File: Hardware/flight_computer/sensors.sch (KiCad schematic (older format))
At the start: 21 parts

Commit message: added components, rerranged things to slow down dan
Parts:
- removed C?: C_10u, Capacitors_SMD:C_0805, symbol openDrone_parts:C_10u
- removed C?: C_0u1, Capacitors_SMD:C_0805, symbol openDrone_parts:C_0u1
- removed C?: C_2u2, Capacitors_SMD:C_0805, symbol openDrone_parts:C_2u2
- removed FL?: EMI_Filter_CLC_100MHZ, drone_footprints:NFL21SP107X1C3D, symbol openDrone_parts:EMI_Filter_CLC_100MHZ
- removed R?: R_220, Resistors_SMD:R_0805, symbol openDrone_parts:R_220
- removed U?: LP5907QMFX-3.3, TO_SOT_Packages_SMD:SOT-23-5, symbol openDrone_parts:LP5907QMFX-3.3
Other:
- note added: "BATTERY = VBAT\nBUCK CONVERTER OUTPUT (VDD_5V_BRICK) = VDD_5V_BUCK\nUSB POWER (VBUS) = VDD_5V_USB\nRADIO 5V (VDD_5V_RECEIVER) = VDD_5V_RADIO\nGENERAL 5V (VDD_5V_IN) = VDD_5V_IN\nTELEM/FRSKY (VDD_5V_PERIPH) = VDD_5V_TELEM\nSTM POWER (FMU_VDD_3V3) = VDD_3V3_STM\nSENSORS POWER (VDD_3V3_SENSORS) = VDD_3V3_SENSORS\nRADIO POWER (VDD_3V3_SPEKTRUM) = RADIO_VDD_3V3\n"
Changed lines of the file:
@@
 $Descr A4 11693 8268
 encoding utf-8
-Sheet 2 4
+Sheet 2 5
 Title ""
 Date ""
@@
 Wire Wire Line
 	8600 2850 8200 2850
-$Comp
-L openDrone_parts:LP5907QMFX-3.3 U?
-U 1 1 5F953D79
-P 9150 4250
-F 0 "U?" H 9150 4617 50  0000 C CNN
-F 1 "LP5907QMFX-3.3" H 9150 4526 50  0000 C CNN
-F 2 "TO_SOT_Packages_SMD:SOT-23-5" H 9150 4600 50  0001 C CNN
-F 3 "http://www.ti.com/lit/ds/symlink/lp5907.pdf" H 9150 4750 50  0001 C CNN
-F 4 "296-40365-1-ND" H 9200 4650 50  0001 C CNN "DPN"
-F 5 "LP5907QMFX-3.3Q1" H 9100 4750 50  0001 C CNN "MPN"
-	1    9150 4250
-	1    0    0    -1
-$EndComp
-$Comp
-L openDrone_parts:R_220 R?
-U 1 1 5F954E14
-P 10150 4300
-F 0 "R?" V 10104 4370 50  0000 L CNN
-F 1 "R_220" V 10195 4370 50  0000 L CNN
-F 2 "Resistors_SMD:R_0805" H 9350 4450 50  0001 C CNN
-F 3 "" H 9850 4800 50  0001 C CNN
-F 4 "311-220CRCT-ND" H 9500 4550 60  0001 C CNN "DPN"
-	1    10150 4300
-	0    1    1    0
-$EndComp
-$Comp
-L openDrone_parts:C_10u C?
-U 1 1 5F9559A3
-P 9900 4300
-F 0 "C?" H 10015 4346 50  0000 L CNN
-F 1 "C_10u" H 10015 4255 50  0000 L CNN
-F 2 "Capacitors_SMD:C_0805" H 9938 4150 50  0001 C CNN
-F 3 "" H 9925 4400 50  0001 C CNN
-F 4 "490-16824-1-ND" H 9900 4300 60  0001 C CNN "DPN"
-	1    9900 4300
-	1    0    0    -1
-$EndComp
-$Comp
-L openDrone_parts:C_0u1 C?
-U 1 1 5F956265
-P 9650 4300
-F 0 "C?" H 9765 4346 50  0000 L CNN
-F 1 "C_0u1" H 9765 4255 50  0000 L CNN
-F 2 "Capacitors_SMD:C_0805" H 9688 4150 50  0001 C CNN
-F 3 "https://www.digikey.com/product-detail/en/kemet/C0805C104Z4VACTU/399-9159-1-ND/3522677" H 9675 4400 50  0001 C CNN
-F 4 "478-3352-1-ND" H 9650 4300 60  0001 C CNN "DPN"
-	1    9650 4300
-	1    0    0    -1
-$EndComp
-$Comp
-L openDrone_parts:C_2u2 C?
-U 1 1 5F956971
-P 8300 4350
-F 0 "C?" H 8415 4396 50  0000 L CNN
-F 1 "C_2u2" H 8415 4305 50  0000 L CNN
-F 2 "Capacitors_SMD:C_0805" H 8338 4200 50  0001 C CNN
-F 3 "" H 8325 4450 50  0001 C CNN
-F 4 "445-13254-1-ND" H 8300 4350 60  0001 C CNN "DPN"
-	1    8300 4350
-	1    0    0    -1
-$EndComp
-Text HLabel 8100 4700 0    50   Input ~ 0
-VDD_3V3_SENSORS_EN
-$Comp
-L power:GND #PWR?
-U 1 1 5F9574AD
-P 9150 4750
-F 0 "#PWR?" H 9150 4500 50  0001 C CNN
-F 1 "GND" H 9155 4577 50  0000 C CNN
-F 2 "" H 9150 4750 50  0001 C CNN
-F 3 "" H 9150 4750 50  0001 C CNN
-	1    9150 4750
-	1    0    0    -1
-$EndComp
-Wire Wire Line
-	9450 4150 9650 4150
-Connection ~ 9650 4150
-Wire Wire Line
-	9650 4150 9900 4150
-Connection ~ 9900 4150
-Wire Wire Line
-	9900 4150 10150 4150
-Connection ~ 10150 4150
-Wire Wire Line
-	10150 4150 10400 4150
-Wire Wire Line
-	10150 4450 9900 4450
-Wire Wire Line
-	9900 4450 9650 4450
-Connection ~ 9900 4450
-Wire Wire Line
-	9650 4450 9650 4650
-Wire Wire Line
-	9650 4650 9150 4650
-Wire Wire Line
-	8300 4650 8300 4500
-Connection ~ 9650 4450
-Wire Wire Line
-	8850 4150 8300 4150
-Wire Wire Line
-	8300 4150 8300 4200
-Wire Wire Line
-	8100 4700 8750 4700
-Wire Wire Line
-	8750 4700 8750 4250
-Wire Wire Line
-	8750 4250 8850 4250
-Wire Wire Line
-	9150 4550 9150 4650
-Connection ~ 9150 4650
-Wire Wire Line
-	9150 4650 8300 4650
-Wire Wire Line
-	9150 4650 9150 4750
-Text HLabel 7250 4150 0    50   Input ~ 0
-VDD_5V
 Text Label 2700 2450 2    50   ~ 0
 VDD_3V3_SENSORS
@@
 VDD_3V3_SENSORS
 Text Label 8200 2850 2    50   ~ 0
-VDD_3V3_SENSORS
-Text Label 10400 4150 0    50   ~ 0
 VDD_3V3_SENSORS
 $Comp
@@
 Text Notes 3100 4000 0    50   ~ 0
 Note for the EMI filter \nthat the GPS here is at 3.3V \nnot 5V like in the pixracer
-$Comp
-L openDrone_parts:EMI_Filter_CLC_100MHZ FL?
-U 1 1 5FA22B48
-P 7800 4250
-F 0 "FL?" H 7800 4567 50  0000 C CNN
-F 1 "EMI_Filter_CLC_100MHZ" H 7800 4476 50  0000 C CNN
-F 2 "drone_footprints:NFL21SP107X1C3D" H 8450 4750 50  0001 C CNN
-F 3 "" V 7800 4250 50  0001 C CNN
-F 4 "490-2540-1-ND" H 8700 4500 50  0001 C CNN "DPN"
-F 5 "NFL21SP107X1C3D" H 8450 4600 50  0001 C CNN "MPN"
-	1    7800 4250
-	1    0    0    -1
-$EndComp
-Wire Wire Line
-	8300 4150 8100 4150
-Connection ~ 8300 4150
-$Comp
-L power:GND #PWR?
-U 1 1 5FA26F34
-P 7800 4350
-F 0 "#PWR?" H 7800 4100 50  0001 C CNN
-F 1 "GND" H 7805 4177 50  0000 C CNN
-F 2 "" H 7800 4350 50  0001 C CNN
-F 3 "" H 7800 4350 50  0001 C CNN
-	1    7800 4350
-	1    0    0    -1
-$EndComp
-Wire Wire Line
-	7250 4150 7500 4150
+Text Notes 7150 6350 0    79   ~ 0
+BATTERY = VBAT\nBUCK CONVERTER OUTPUT (VDD_5V_BRICK) = VDD_5V_BUCK\nUSB POWER (VBUS) = VDD_5V_USB\nRADIO 5V (VDD_5V_RECEIVER) = VDD_5V_RADIO\nGENERAL 5V (VDD_5V_IN) = VDD_5V_IN\nTELEM/FRSKY (VDD_5V_PERIPH) = VDD_5V_TELEM\nSTM POWER (FMU_VDD_3V3) =  VDD_3V3_STM\nSENSORS POWER (VDD_3V3_SENSORS) = VDD_3V3_SENSORS\nRADIO POWER  (VDD_3V3_SPEKTRUM) = RADIO_VDD_3V3\n
 $EndSCHEMATC

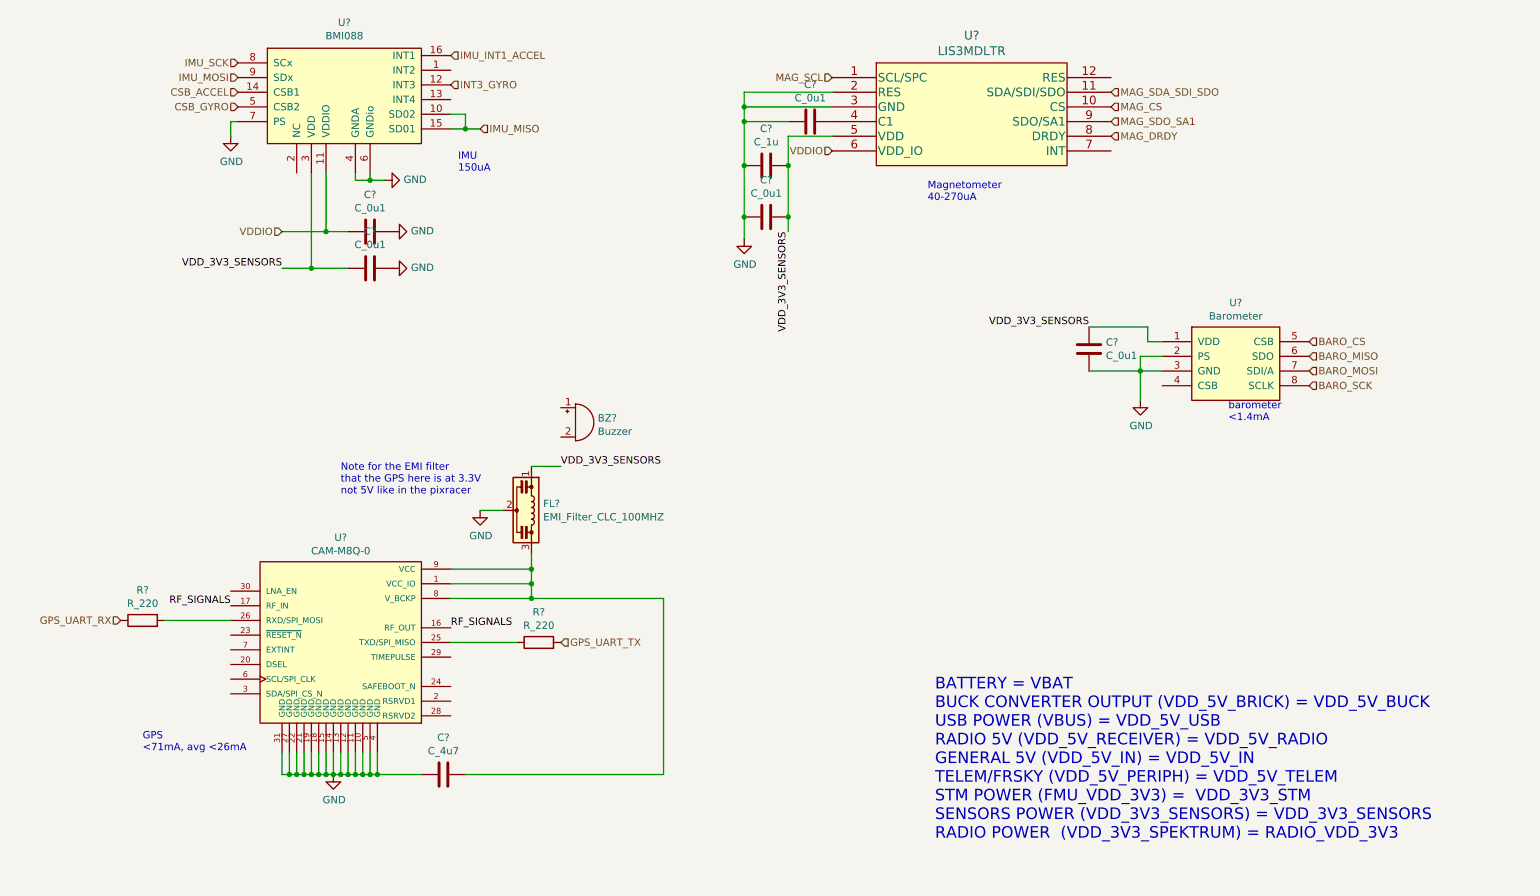
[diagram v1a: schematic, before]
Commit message: added more components, added buzzer, servo circuits, re-arranged some power
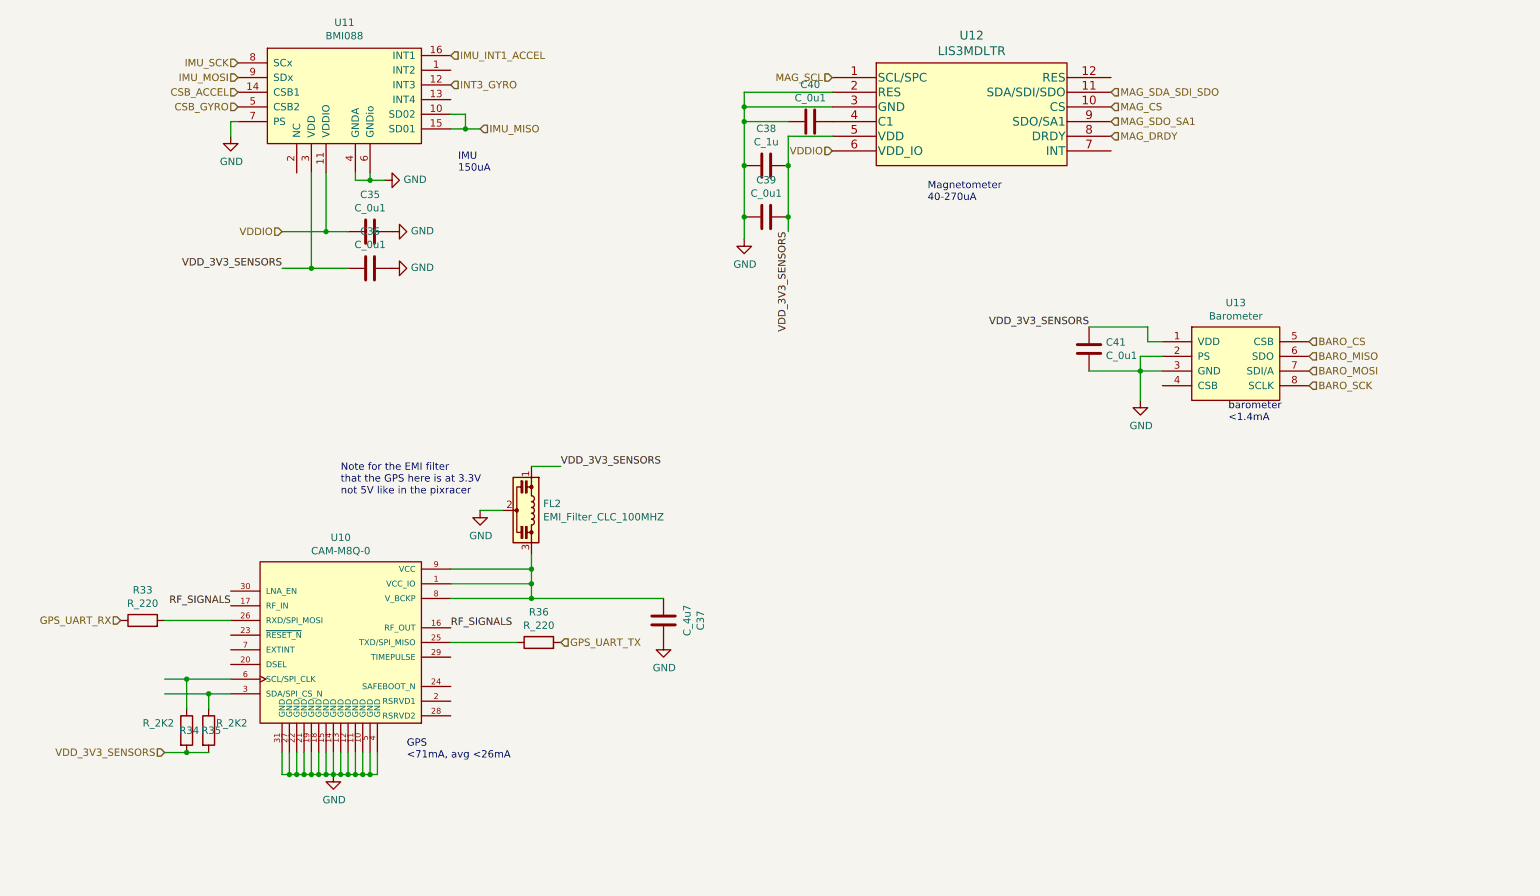
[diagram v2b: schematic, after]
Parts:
- removed BZ?: Buzzer, drone_footprints:PT-2040PQ, symbol openDrone_parts:Buzzer
- added R34, R35: R_2K2, Resistors_SMD:R_0805, symbol openDrone_parts:R_2K2
- gave numbers to parts that had none: 14
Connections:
- net GND: now also C37.1; no longer C37.2
- net VDD_3V3_SENSORS: now also R34.2, R35.2
- net at FL2.3, U10.1 (VCC_IO), U10.8 (V_BCKP)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: now also C37.2; no longer C37.1
- net at U10.3 (SDA/SPI_CS_N): now also R35.1
- net at U10.6 (SCL/SPI_CLK): now also R34.1
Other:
- note removed: "BATTERY = VBAT\nBUCK CONVERTER OUTPUT (VDD_5V_BRICK) = VDD_5V_BUCK\nUSB POWER (VBUS) = VDD_5V_USB\nRADIO 5V (VDD_5V_RECEIVER) = VDD_5V_RADIO\nGENERAL 5V (VDD_5V_IN) = VDD_5V_IN\nTELEM/FRSKY (VDD_5V_PERIPH) = VDD_5V_TELEM\nSTM POWER (FMU_VDD_3V3) = VDD_3V3_STM\nSENSORS POWER (VDD_3V3_SENSORS) = VDD_3V3_SENSORS\nRADIO POWER (VDD_3V3_SPEKTRUM) = RADIO_VDD_3V3\n"
- moved on the sheet: C37
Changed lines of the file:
@@
 $Descr A4 11693 8268
 encoding utf-8
-Sheet 2 5
+Sheet 5 4
 Title ""
 Date ""
@@
 $EndDescr
 $Comp
-L openDrone_parts:BMI088 U?
+L openDrone_parts:BMI088 U11
 U 1 1 5F91431C
 P 3700 1150
-F 0 "U?" H 3125 1525 50  0000 C CNN
+F 0 "U11" H 3125 1525 50  0000 C CNN
 F 1 "BMI088" H 3125 1434 50  0000 C CNN
 F 2 "drone_footprints:BMI088" H 3600 1450 50  0001 C CNN
@@
 $EndComp
 $Comp
-L openDrone_parts:C_0u1 C?
+L openDrone_parts:C_0u1 C35
 U 1 1 5F915123
 P 3300 2200
-F 0 "C?" V 3048 2200 50  0000 C CNN
+F 0 "C35" V 3048 2200 50  0000 C CNN
 F 1 "C_0u1" V 3139 2200 50  0000 C CNN
 F 2 "Capacitors_SMD:C_0805" H 3338 2050 50  0001 C CNN
@@
 $EndComp
 $Comp
-L openDrone_parts:C_0u1 C?
+L openDrone_parts:C_0u1 C36
 U 1 1 5F918639
 P 3300 2450
-F 0 "C?" V 3552 2450 50  0000 C CNN
+F 0 "C36" V 3552 2450 50  0000 C CNN
 F 1 "C_0u1" V 3461 2450 50  0000 C CNN
 F 2 "Capacitors_SMD:C_0805" H 3338 2300 50  0001 C CNN
@@
 CSB_GYRO
 $Comp
-L power:GND #PWR?
+L power:GND #PWR047
 U 1 1 5F919457
 P 2350 1550
-F 0 "#PWR?" H 2350 1300 50  0001 C CNN
+F 0 "#PWR047" H 2350 1300 50  0001 C CNN
 F 1 "GND" H 2355 1377 50  0000 C CNN
 F 2 "" H 2350 1550 50  0001 C CNN
@@
 	3950 1500 4050 1500
 $Comp
-L power:GND #PWR?
+L power:GND #PWR049
 U 1 1 5F920805
 P 3400 1850
-F 0 "#PWR?" H 3400 1600 50  0001 C CNN
+F 0 "#PWR049" H 3400 1600 50  0001 C CNN
 F 1 "GND" V 3405 1722 50  0000 R CNN
 F 2 "" H 3400 1850 50  0001 C CNN
@@
 	2900 2450 3150 2450
 $Comp
-L power:GND #PWR?
+L power:GND #PWR050
 U 1 1 5F92AF4D
 P 3450 2200
-F 0 "#PWR?" H 3450 1950 50  0001 C CNN
+F 0 "#PWR050" H 3450 1950 50  0001 C CNN
 F 1 "GND" V 3455 2072 50  0000 R CNN
 F 2 "" H 3450 2200 50  0001 C CNN
@@
 $EndComp
 $Comp
-L power:GND #PWR?
+L power:GND #PWR051
 U 1 1 5F92B1B3
 P 3450 2450
-F 0 "#PWR?" H 3450 2200 50  0001 C CNN
+F 0 "#PWR051" H 3450 2200 50  0001 C CNN
 F 1 "GND" V 3455 2322 50  0000 R CNN
 F 2 "" H 3450 2450 50  0001 C CNN
@@
 VDDIO
 $Comp
-L power:GND #PWR?
+L power:GND #PWR054
 U 1 1 5F9483AF
 P 5850 2250
-F 0 "#PWR?" H 5850 2000 50  0001 C CNN
+F 0 "#PWR054" H 5850 2000 50  0001 C CNN
 F 1 "GND" H 5855 2077 50  0000 C CNN
 F 2 "" H 5850 2250 50  0001 C CNN
@@
 MAG_SCL
 $Comp
-L openDrone_parts:C_0u1 C?
+L openDrone_parts:C_0u1 C40
 U 1 1 5F949212
 P 6300 1450
-F 0 "C?" V 6048 1450 50  0000 C CNN
+F 0 "C40" V 6048 1450 50  0000 C CNN
 F 1 "C_0u1" V 6139 1450 50  0000 C CNN
 F 2 "Capacitors_SMD:C_0805" H 6338 1300 50  0001 C CNN
@@
 $EndComp
 $Comp
-L openDrone_parts:C_0u1 C?
+L openDrone_parts:C_0u1 C39
 U 1 1 5F94A2A0
 P 6000 2100
-F 0 "C?" V 5748 2100 50  0000 C CNN
+F 0 "C39" V 5748 2100 50  0000 C CNN
 F 1 "C_0u1" V 5839 2100 50  0000 C CNN
 F 2 "Capacitors_SMD:C_0805" H 6038 1950 50  0001 C CNN
@@
 $EndComp
 $Comp
-L openDrone_parts:C_1u C?
+L openDrone_parts:C_1u C38
 U 1 1 5F94ABD0
 P 6000 1750
-F 0 "C?" V 5748 1750 50  0000 C CNN
+F 0 "C38" V 5748 1750 50  0000 C CNN
 F 1 "C_1u" V 5839 1750 50  0000 C CNN
 F 2 "Capacitors_SMD:C_0805" H 6038 1600 50  0001 C CNN
@@
 Connection ~ 5850 1350
 $Comp
-L openDrone_parts:Barometer U?
+L openDrone_parts:Barometer U13
 U 1 1 5F94F59C
 P 9100 2950
-F 0 "U?" H 9200 3215 50  0000 C CNN
+F 0 "U13" H 9200 3215 50  0000 C CNN
 F 1 "Barometer" H 9200 3124 50  0000 C CNN
 F 2 "drone_footprints:MS561101BA03-50" H 9500 3300 50  0001 C CNN
@@
 BARO_SCK
 $Comp
-L power:GND #PWR?
+L power:GND #PWR055
 U 1 1 5F95039A
 P 8550 3350
-F 0 "#PWR?" H 8550 3100 50  0001 C CNN
+F 0 "#PWR055" H 8550 3100 50  0001 C CNN
 F 1 "GND" H 8555 3177 50  0000 C CNN
 F 2 "" H 8550 3350 50  0001 C CNN
@@
 $EndComp
 $Comp
-L openDrone_parts:C_0u1 C?
+L openDrone_parts:C_0u1 C41
 U 1 1 5F950BFE
 P 8200 3000
-F 0 "C?" H 8315 3046 50  0000 L CNN
+F 0 "C41" H 8315 3046 50  0000 L CNN
 F 1 "C_0u1" H 8315 2955 50  0000 L CNN
 F 2 "Capacitors_SMD:C_0805" H 8238 2850 50  0001 C CNN
@@
 VDD_3V3_SENSORS
 $Comp
-L openDrone_parts:Buzzer BZ?
-U 1 1 5F827564
-P 4700 3500
-F 0 "BZ?" H 4852 3529 50  0000 L CNN
-F 1 "Buzzer" H 4852 3438 50  0000 L CNN
-F 2 "drone_footprints:PT-2040PQ" H 5050 3950 50  0001 C CNN
-F 3 "~" V 4675 3600 50  0001 C CNN
-F 4 "458-1078-ND" H 5000 3750 50  0001 C CNN "DPN"
-F 5 "PT-2040PQ" H 4950 3850 50  0001 C CNN "MPN"
-	1    4700 3500
-	1    0    0    -1
-$EndComp
-$Comp
-L openDrone_parts:CAM-M8Q-0 U?
+L openDrone_parts:CAM-M8Q-0 U10
 U 1 1 5F827FBC
 P 3100 4600
-F 0 "U?" H 3100 4915 50  0000 C CNN
+F 0 "U10" H 3100 4915 50  0000 C CNN
 F 1 "CAM-M8Q-0" H 3100 4824 50  0000 C CNN
 F 2 "drone_footprints:CAM_M8Q_0" H 2650 4950 50  0001 L BNN
@@
 $EndComp
 $Comp
-L openDrone_parts:R_220 R?
+L openDrone_parts:R_220 R36
 U 1 1 5F82A212
 P 4450 5000
-F 0 "R?" H 4450 5207 50  0000 C CNN
+F 0 "R36" H 4450 5207 50  0000 C CNN
 F 1 "R_220" H 4450 5116 50  0000 C CNN
 F 2 "Resistors_SMD:R_0805" H 3650 5150 50  0001 C CNN
@@
 $EndComp
 $Comp
-L openDrone_parts:R_220 R?
+L openDrone_parts:R_220 R33
 U 1 1 5F82B7EB
 P 1750 4850
-F 0 "R?" H 1750 5057 50  0000 C CNN
+F 0 "R33" H 1750 5057 50  0000 C CNN
 F 1 "R_220" H 1750 4966 50  0000 C CNN
 F 2 "Resistors_SMD:R_0805" H 950 5000 50  0001 C CNN
@@
 GPS_UART_RX
 $Comp
-L power:GND #PWR?
+L power:GND #PWR048
 U 1 1 5F857A76
 P 3050 5900
-F 0 "#PWR?" H 3050 5650 50  0001 C CNN
+F 0 "#PWR048" H 3050 5650 50  0001 C CNN
 F 1 "GND" H 3055 5727 50  0000 C CNN
 F 2 "" H 3050 5900 50  0001 C CNN
@@
 Connection ~ 4400 4600
 $Comp
-L openDrone_parts:C_4u7 C?
+L openDrone_parts:C_4u7 C37
 U 1 1 5F87B412
-P 3800 5900
-F 0 "C?" V 3548 5900 50  0000 C CNN
-F 1 "C_4u7" V 3639 5900 50  0000 C CNN
-F 2 "Capacitors_SMD:C_0805" H 3838 5750 50  0001 C CNN
-F 3 "" H 3825 6000 50  0001 C CNN
-F 4 "490-14466-1-ND" H 3800 5900 60  0001 C CNN "DPN"
-	1    3800 5900
-	0    1    1    0
-$EndComp
-Wire Wire Line
-	3350 5900 3650 5900
-Connection ~ 3350 5900
-Wire Wire Line
-	3950 5900 5300 5900
-Wire Wire Line
-	5300 5900 5300 4700
+P 5300 4850
+F 0 "C37" V 5048 4850 50  0000 C CNN
+F 1 "C_4u7" V 5139 4850 50  0000 C CNN
+F 2 "Capacitors_SMD:C_0805" H 5338 4700 50  0001 C CNN
+F 3 "" H 5325 4950 50  0001 C CNN
+F 4 "490-14466-1-ND" H 5300 4850 60  0001 C CNN "DPN"
+	1    5300 4850
+	-1   0    0    1
+$EndComp
 Wire Wire Line
 	5300 4700 4400 4700
 Connection ~ 4400 4700
 $Comp
-L openDrone_parts:LIS3MDLTR U?
+L openDrone_parts:LIS3MDLTR U12
 U 1 1 5F9477A8
 P 6450 1150
-F 0 "U?" H 7400 1437 60  0000 C CNN
+F 0 "U12" H 7400 1437 60  0000 C CNN
 F 1 "LIS3MDLTR" H 7400 1331 60  0000 C CNN
 F 2 "drone_footprints:LIS3MDLTR" H 7650 1390 60  0001 C CNN
@@
 Text Notes 3900 1800 0    50   ~ 0
 IMU\n150uA
-Text Notes 1750 5750 0    50   ~ 0
+Text Notes 3550 5800 0    50   ~ 0
 GPS\n<71mA, avg <26mA
 Text Notes 9150 3500 0    50   ~ 0
 barometer\n<1.4mA
 $Comp
-L openDrone_parts:EMI_Filter_CLC_100MHZ FL?
+L openDrone_parts:EMI_Filter_CLC_100MHZ FL2
 U 1 1 5F9362EA
 P 4300 4100
-F 0 "FL?" V 4254 4280 50  0000 L CNN
+F 0 "FL2" V 4254 4280 50  0000 L CNN
 F 1 "EMI_Filter_CLC_100MHZ" V 4345 4280 50  0000 L CNN
 F 2 "drone_footprints:NFL21SP107X1C3D" H 4950 4600 50  0001 C CNN
@@
 	4600 3800 4400 3800
 $Comp
-L power:GND #PWR?
+L power:GND #PWR052
 U 1 1 5F93AFA7
 P 4050 4100
-F 0 "#PWR?" H 4050 3850 50  0001 C CNN
+F 0 "#PWR052" H 4050 3850 50  0001 C CNN
 F 1 "GND" H 4055 3927 50  0000 C CNN
 F 2 "" H 4050 4100 50  0001 C CNN
@@
 Text Notes 3100 4000 0    50   ~ 0
 Note for the EMI filter \nthat the GPS here is at 3.3V \nnot 5V like in the pixracer
-Text Notes 7150 6350 0    79   ~ 0
-BATTERY = VBAT\nBUCK CONVERTER OUTPUT (VDD_5V_BRICK) = VDD_5V_BUCK\nUSB POWER (VBUS) = VDD_5V_USB\nRADIO 5V (VDD_5V_RECEIVER) = VDD_5V_RADIO\nGENERAL 5V (VDD_5V_IN) = VDD_5V_IN\nTELEM/FRSKY (VDD_5V_PERIPH) = VDD_5V_TELEM\nSTM POWER (FMU_VDD_3V3) =  VDD_3V3_STM\nSENSORS POWER (VDD_3V3_SENSORS) = VDD_3V3_SENSORS\nRADIO POWER  (VDD_3V3_SPEKTRUM) = RADIO_VDD_3V3\n
+$Comp
+L power:GND #PWR053
+U 1 1 5FB16EE2
+P 5300 5000
+F 0 "#PWR053" H 5300 4750 50  0001 C CNN
+F 1 "GND" H 5305 4827 50  0000 C CNN
+F 2 "" H 5300 5000 50  0001 C CNN
+F 3 "" H 5300 5000 50  0001 C CNN
+	1    5300 5000
+	1    0    0    -1
+$EndComp
+Wire Wire Line
+	2350 5250 2050 5250
+Wire Wire Line
+	2350 5350 2200 5350
+$Comp
+L openDrone_parts:R_2K2 R34
+U 1 1 5FB1C59E
+P 2050 5600
+F 0 "R34" V 2050 5550 50  0000 L CNN
+F 1 "R_2K2" V 2000 5300 50  0000 L CNN
+F 2 "Resistors_SMD:R_0805" H 2500 5900 50  0001 C CNN
+F 3 "" H 1750 6100 50  0001 C CNN
+F 4 "RMCF0805JT2K20CT-ND" H 2700 6100 60  0001 C CNN "DPN"
+F 5 "RMCF0805JT2K20" H 2500 6000 50  0001 C CNN "MPN"
+	1    2050 5600
+	0    1    1    0
+$EndComp
+$Comp
+L openDrone_parts:R_2K2 R35
+U 1 1 5FB1D219
+P 2200 5600
+F 0 "R35" V 2200 5550 50  0000 L CNN
+F 1 "R_2K2" V 2150 5650 50  0000 L CNN
+F 2 "Resistors_SMD:R_0805" H 2650 5900 50  0001 C CNN
+F 3 "" H 1900 6100 50  0001 C CNN
+F 4 "RMCF0805JT2K20CT-ND" H 2850 6100 60  0001 C CNN "DPN"
+F 5 "RMCF0805JT2K20" H 2650 6000 50  0001 C CNN "MPN"
+	1    2200 5600
+	0    1    1    0
+$EndComp
+Wire Wire Line
+	2200 5350 2200 5450
+Wire Wire Line
+	2050 5250 2050 5450
+Wire Wire Line
+	2200 5350 1900 5350
+Connection ~ 2200 5350
+Wire Wire Line
+	2050 5250 1900 5250
+Connection ~ 2050 5250
+Text HLabel 1900 5750 0    50   Input ~ 0
+VDD_3V3_SENSORS
+Wire Wire Line
+	1900 5750 2050 5750
+Connection ~ 2050 5750
+Wire Wire Line
+	2050 5750 2200 5750
 $EndSCHEMATC

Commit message: Finishes v1 connections
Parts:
- removed R34, R35: R_2K2, Resistors_SMD:R_0805, symbol openDrone_parts:R_2K2
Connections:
- net VDDIO is gone; now on net VDD_3V3_SENSORS: C35.2, U11.11 (VDDIO), U12.6 (VDD_IO)
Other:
- note added: "BAROMETER"
- note added: "Check VDDIO connection"
- note added: "GPS MODULE"
- note added: "IMU"
- note added: "MAGNETOMETER"
- moved on the sheet: C35, C36, C37, C38, C39, C40, C41, FL2, R33, R36, U10, U11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
